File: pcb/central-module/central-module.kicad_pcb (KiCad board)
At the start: 2 copper layers, 100 x 100 mm, 32 parts, among them J1 Conn_01x10_Pin, J2 Screw_Terminal_01x04, J3 Conn_01x04_Pin, J4 Screw_Terminal_01x03, J5 Screw_Terminal_01x04, Q1 IRF3205, U1 ESP32_DEVCITV1, U2 74HC245

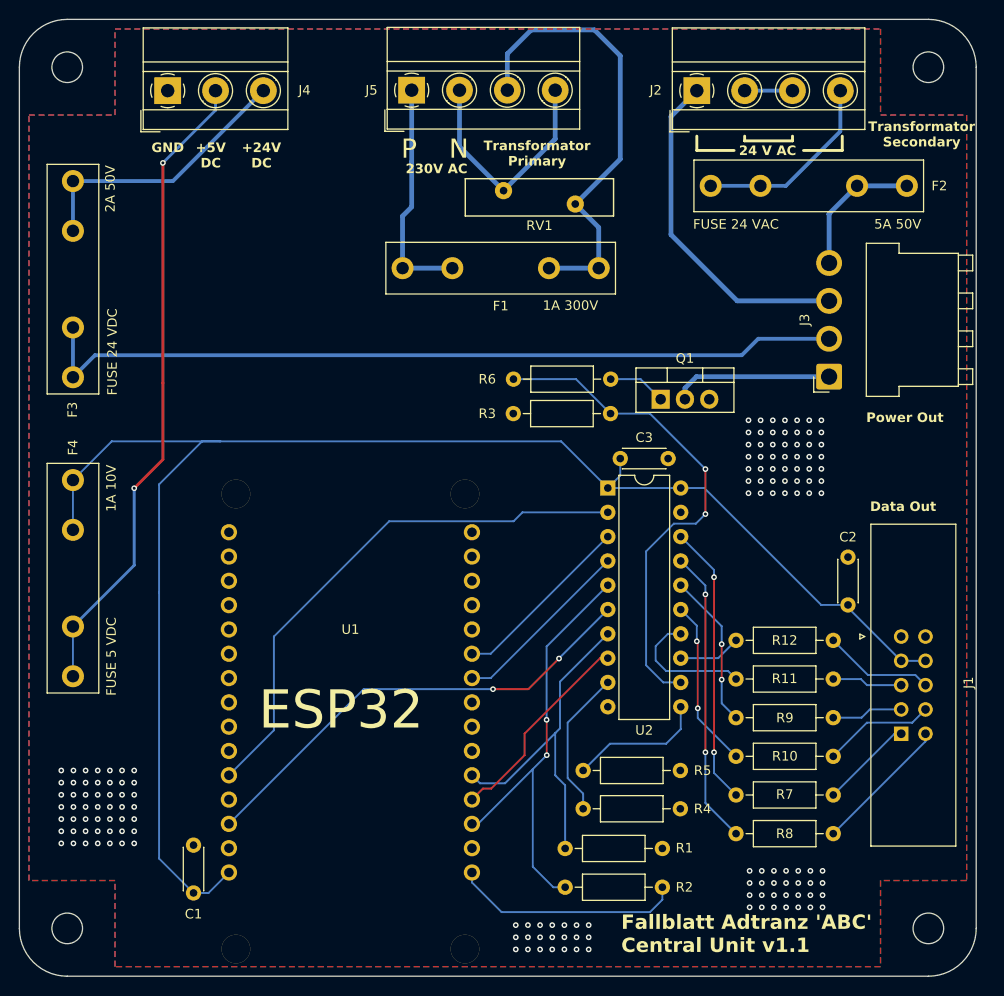
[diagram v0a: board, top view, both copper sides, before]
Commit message: full 20 module current measurement and fuses
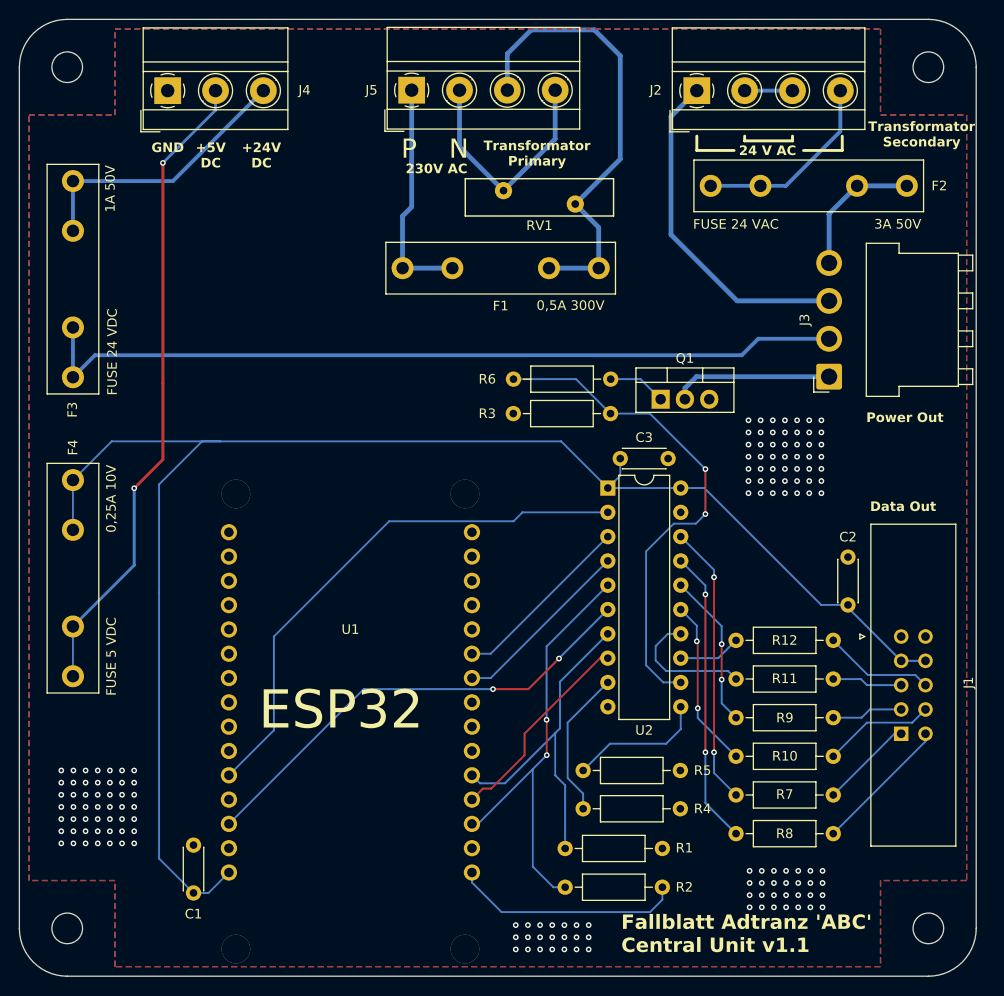
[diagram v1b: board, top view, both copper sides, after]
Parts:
- F1: value 1A 300V -> 0,5A 300V
- F2: value 5A 50V -> 3A 50V
- F3: value 2A 50V -> 1A 50V
- F4: value 1A 10V -> 0,25A 10V
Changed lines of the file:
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@@
 			)
 		)
-		(property "Value" "2A 50V"
+		(property "Value" "1A 50V"
 			(at 0.8 -3.9 90)
 			(unlocked yes)
@@
 			)
 		)
-		(property "Value" "1A 10V"
-			(at 19.65 4 90)
+		(property "Value" "0,25A 10V"
+			(at 18.55 4 90)
 			(unlocked yes)
 			(layer "F.SilkS")
@@
 			)
 		)
-		(property "Value" "1A 300V"
+		(property "Value" "0,5A 300V"
 			(at 2.95 -3.9 0)
 			(unlocked yes)
@@
 			)
 		)
-		(property "Value" "5A 50V"
+		(property "Value" "3A 50V"
 			(at 19.55 4 0)
 			(unlocked yes)
@@
 		(min_thickness 0.25)
 		(filled_areas_thickness no)
-		(fill yes
+		(fill
 			(thermal_gap 0.5)
 			(thermal_bridge_width 0.5)

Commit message: new terminal blocks 7.5 and schurter fuseholders
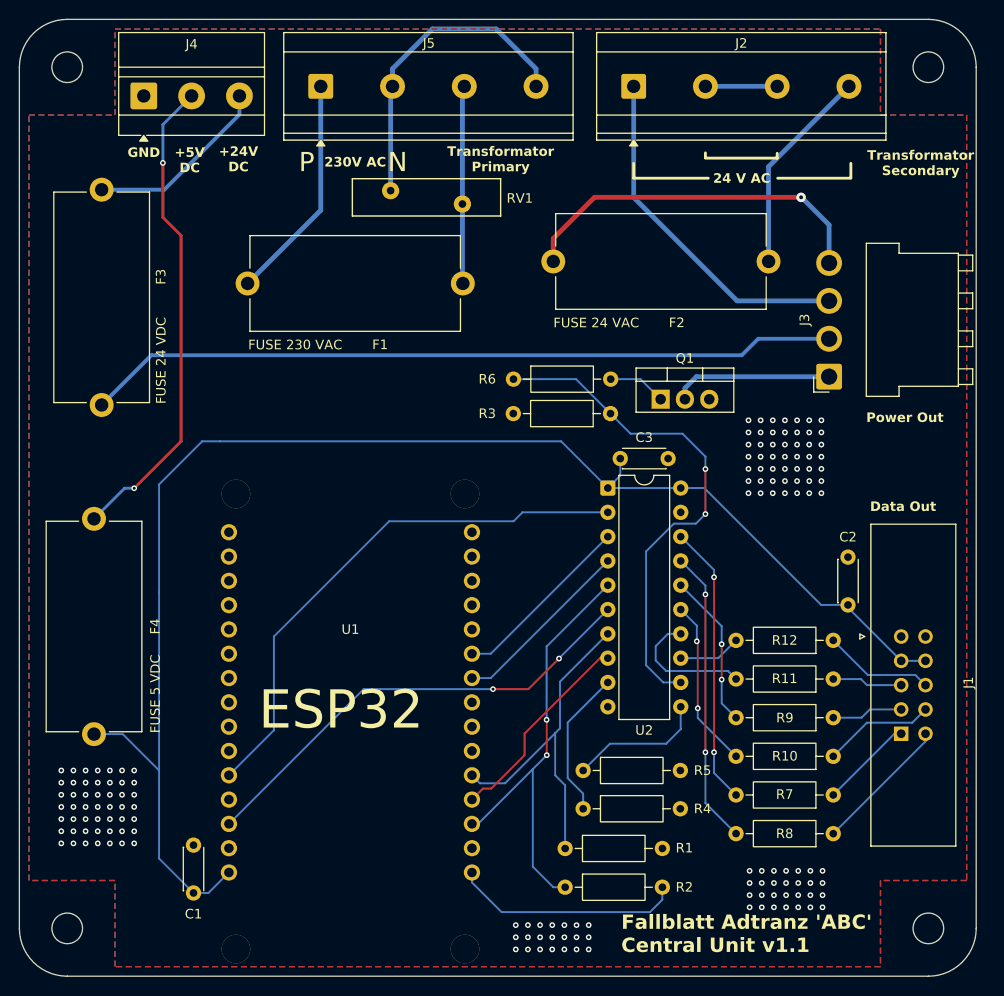
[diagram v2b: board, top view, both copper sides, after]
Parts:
- F1, F2, F3, F4: footprint Fuse:Fuseholder_Littelfuse_445_030_series_5x20mm -> JS_Local:Fuseholder_Schurter_OGN_22.5
- J2, J5: footprint TerminalBlock_MetzConnect:TerminalBlock_MetzConnect_Type011_RT05504HBWC_1x04_P5.00mm_Horizontal -> TerminalBlock_MetzConnect:TerminalBlock_MetzConnect_Type175_RT02704HBLC_1x04_P7.50mm_Horizontal
- J4: footprint TerminalBlock_MetzConnect:TerminalBlock_MetzConnect_Type011_RT05503HBWC_1x03_P5.00mm_Horizontal -> TerminalBlock_MetzConnect:TerminalBlock_MetzConnect_Type011_RT05503HBLC_1x03_P5.00mm_Horizontal
- R11: value ?? -> 47
- moved F1 25.5 mm to (135.1, 77.6), turned to 0 degrees
- moved F3 12.5 mm to (108.6, 79.0), turned to 90 degrees
- moved RV1 11.8 mm to (138.8, 67.9)
- moved J5 9.51 mm to (131.5, 57.0)
- moved F2 9.46 mm to (167.1, 75.3)
- moved J2 6.62 mm to (164.2, 57.0)
- moved F4 5.65 mm to (107.8, 113.5)
- moved J4 2.56 mm to (113.0, 58.0)
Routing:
- net /P_FUSED: track 48.1 -> 20.7 mm
- net /24VAC_P: track 14.5 -> 38.2 mm, vias 0 -> 1
- net Net-(J4-Pin_2): track 67.4 -> 50.6 mm
- net +5V: track 166.3 -> 152.4 mm
- net /+24V_UF: track 29.0 -> 19.6 mm
- net /N: track 25.1 -> 33.1 mm
- net +24V: track 85.9 -> 78.9 mm
- net /T_BRIDGE: track 5.00 -> 7.50 mm
- net /24VAC_P_UF: track 20.2 -> 21.8 mm
- net /24VAC_N: track 35.6 -> 36.5 mm
- net DC_PWR: track 52.7 -> 53.5 mm
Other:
- board text added: "FUSE 230 VAC"

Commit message: central module final v1.1
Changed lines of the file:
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@@
 			(drillshape 0)
 			(scaleselection 1)
-			(outputdirectory "gerber/")
+			(outputdirectory "gerber-v1.1/")
 		)
 	)
@@
 			)
 		)
-		(property "Datasheet" ""
+		(property "Datasheet" "~"
 			(at 0 0 90)
 			(unlocked yes)
@@
 			)
 		)
-		(property "Datasheet" ""
+		(property "Datasheet" "~"
 			(at 0 0 270)
 			(unlocked yes)
@@
 		(attr through_hole)
 		(fp_line
-			(start 0.23 1.07)
-			(end 4.77 1.07)
+			(start 4.77 1.07)
+			(end 0.23 1.07)
 			(stroke
 				(width 0.12)
@@
 		)
 		(fp_line
-			(start 0.23 1.014)
-			(end 0.23 1.07)
+			(start 4.77 1.014)
+			(end 4.77 1.07)
 			(stroke
 				(width 0.12)
@@
 		)
 		(fp_line
-			(start 4.77 1.014)
-			(end 4.77 1.07)
+			(start 0.23 -1.014)
+			(end 0.23 -1.07)
 			(stroke
 				(width 0.12)
@@
 			)
 		)
-		(property "Datasheet" ""
+		(property "Datasheet" "~"
 			(at 0 0 90)
 			(unlocked yes)
@@
 			)
 		)
-		(property "Datasheet" ""
+		(property "Datasheet" "~"
 			(at 0 0 0)
 			(layer "F.Fab")
@@
 			)
 		)
-		(property "Datasheet" ""
+		(property "Datasheet" "~"
 			(at 0 0 0)
 			(layer "F.Fab")
@@
 			)
 		)
-		(property "Datasheet" ""
+		(property "Datasheet" "~"
 			(at 0 0 270)
 			(unlocked yes)
@@
 		(attr through_hole)
 		(fp_line
-			(start 0.23 1.07)
-			(end 4.77 1.07)
+			(start 4.77 1.07)
+			(end 0.23 1.07)
 			(stroke
 				(width 0.12)
@@
 		)
 		(fp_line
-			(start 0.23 1.014)
-			(end 0.23 1.07)
+			(start 4.77 1.014)
+			(end 4.77 1.07)
 			(stroke
 				(width 0.12)
@@
 		)
 		(fp_line
-			(start 4.77 1.014)
-			(end 4.77 1.07)
+			(start 0.23 -1.014)
+			(end 0.23 -1.07)
 			(stroke
 				(width 0.12)
@@
 			)
 		)
-		(property "Datasheet" ""
+		(property "Datasheet" "~"
 			(at 0 0 0)
 			(layer "F.Fab")
@@
 			)
 		)
-		(property "Datasheet" ""
+		(property "Datasheet" "~"
 			(at 0 0 180)
 			(unlocked yes)
@@
 			)
 		)
-		(property "Datasheet" ""
+		(property "Datasheet" "~"
 			(at 0 0 0)
 			(unlocked yes)
@@
 			)
 		)
-		(property "Datasheet" ""
+		(property "Datasheet" "~"
 			(at 0 0 0)
 			(unlocked yes)
@@
 			)
 		)
-		(property "Datasheet" ""
+		(property "Datasheet" "~"
 			(at 0 0 0)
 			(unlocked yes)
@@
 		)
 		(fp_line
-			(start 0.23 1.014)
-			(end 0.23 1.07)
+			(start 0.23 -1.014)
+			(end 0.23 -1.07)
 			(stroke
 				(width 0.12)
@@
 		)
 		(fp_line
-			(start 0.23 1.07)
+			(start 4.77 1.014)
 			(end 4.77 1.07)
 			(stroke
@@
 		)
 		(fp_line
-			(start 4.77 1.014)
-			(end 4.77 1.07)
+			(start 4.77 1.07)
+			(end 0.23 1.07)
 			(stroke
 				(width 0.12)
@@
 			)
 		)
-		(property "Datasheet" ""
+		(property "Datasheet" "~"
 			(at 0 0 0)
 			(unlocked yes)
@@
 			)
 		)
-		(property "Datasheet" ""
+		(property "Datasheet" "~"
 			(at 0 0 0)
 			(unlocked yes)
@@
 			)
 		)
-		(property "Datasheet" ""
+		(property "Datasheet" "~"
 			(at 0 0 90)
 			(unlocked yes)
@@
 			)
 		)
-		(property "Datasheet" ""
+		(property "Datasheet" "~"
 			(at 0 0 180)
 			(unlocked yes)
@@
 			)
 		)
-		(property "Datasheet" ""
+		(property "Datasheet" "~"
 			(at 0 0 0)
 			(unlocked yes)
@@
 			)
 		)
-		(property "Datasheet" ""
+		(property "Datasheet" "~"
 			(at 0 0 180)
 			(unlocked yes)
@@
 			)
 		)
-		(property "Datasheet" ""
+		(property "Datasheet" "~"
 			(at 0 0 180)
 			(unlocked yes)
@@
 			)
 		)
-		(property "Datasheet" ""
+		(property "Datasheet" "~"
 			(at 0 0 0)
 			(unlocked yes)
@@
 			)
 		)
-		(property "Datasheet" ""
+		(property "Datasheet" "~"
 			(at 0 0 0)
 			(unlocked yes)
@@
 			)
 		)
-		(property "Datasheet" ""
+		(property "Datasheet" "~"
 			(at 0 0 0)
 			(layer "F.Fab")
@@
 			)
 		)
-		(property "Datasheet" ""
+		(property "Datasheet" "~"
 			(at 0 0 180)
 			(unlocked yes)
@@
 			)
 		)
-		(property "Datasheet" ""
+		(property "Datasheet" "~"
 			(at 0 0 0)
 			(unlocked yes)
@@
 			)
 		)
-		(property "Sim.Library" "${KICAD7_SYMBOL_DIR}/Simulation_SPICE.sp"
+		(property "Sim.Library" "${KICAD9_SYMBOL_DIR}/Simulation_SPICE.sp"
 			(at 0 0 0)
 			(unlocked yes)
@@
 			)
 		)
-		(property "Datasheet" ""
+		(property "Datasheet" "~"
 			(at 0 0 180)
 			(unlocked yes)
@@
 		(sheetfile "central-module.kicad_sch")
 		(attr through_hole)
+		(fp_rect
+			(start -2 -6.5)
+			(end 27.5 46.5)
+			(stroke
+				(width 0.05)
+				(type default)
+			)
+			(fill no)
+			(layer "B.CrtYd")
+		)
 		(fp_line
 			(start -1.27 0)
@@
 			(layer "F.Fab")
 		)
-		(pad "" thru_hole circle
+		(pad "" np_thru_hole circle
 			(at 0.73 -4)
 			(size 3 3)
 			(drill 3)
 			(layers "*.Cu" "*.Mask")
-			(remove_unused_layers no)
 		)
-		(pad "" thru_hole circle
+		(pad "" np_thru_hole circle
 			(at 0.73 43.56)
 			(size 3 3)
 			(drill 3)
 			(layers "*.Cu" "*.Mask")
-			(remove_unused_layers no)
 		)
-		(pad "" thru_hole circle
+		(pad "" np_thru_hole circle
 			(at 24.67 -4)
 			(size 3 3)
 			(drill 3)
 			(layers "*.Cu" "*.Mask")
-			(remove_unused_layers no)
 		)
-		(pad "" thru_hole circle
+		(pad "" np_thru_hole circle
 			(at 24.67 43.56)
 			(size 3 3)
 			(drill 3)
 			(layers "*.Cu" "*.Mask")
-			(remove_unused_layers no)
 		)
 		(pad "1" thru_hole circle
@@
 			)
 		)
-		(property "Datasheet" ""
+		(property "Datasheet" "~"
 			(at 0 0 180)
 			(unlocked yes)
